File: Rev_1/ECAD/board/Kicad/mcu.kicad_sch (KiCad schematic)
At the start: 11 parts, among them Y100 16MHZ

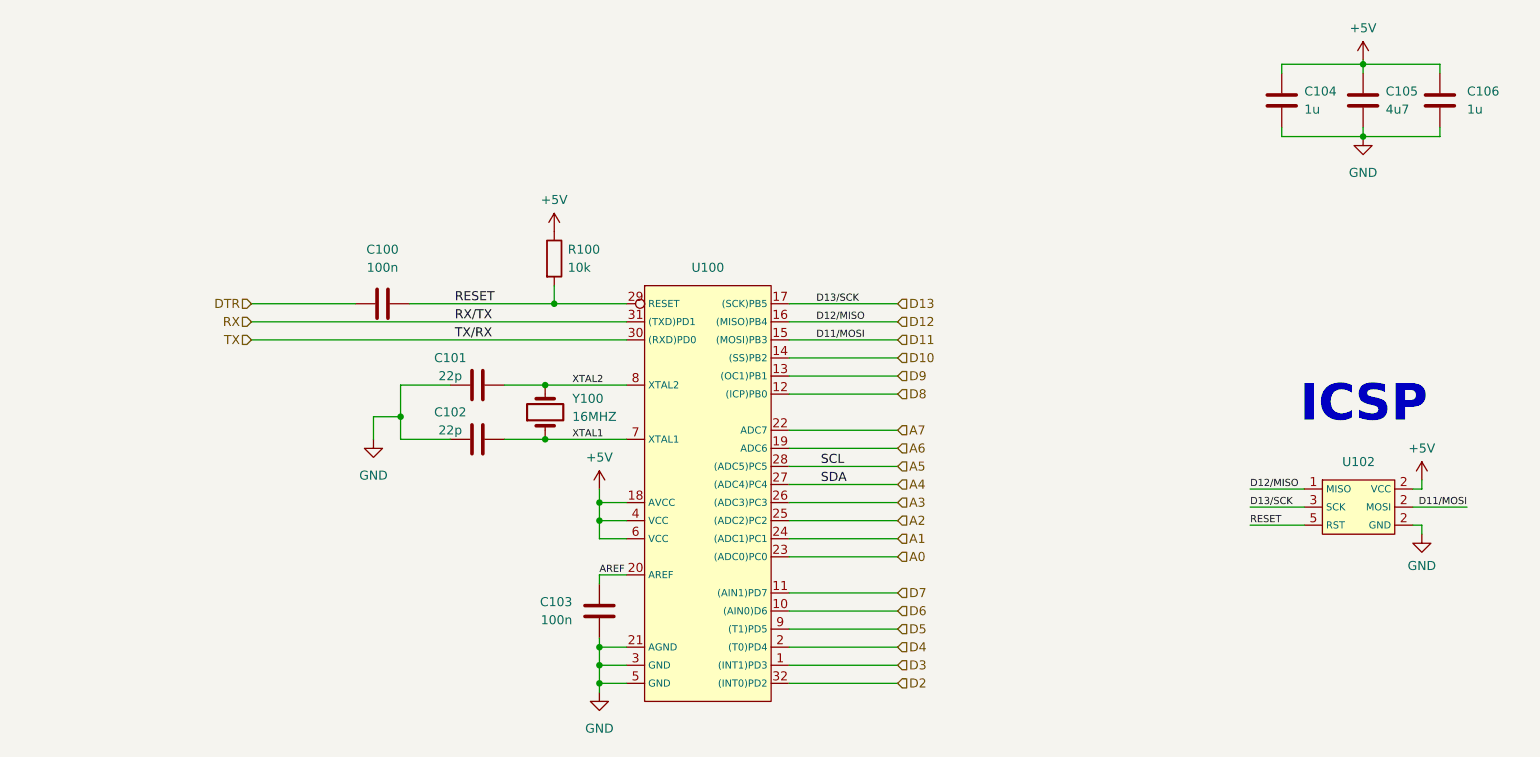
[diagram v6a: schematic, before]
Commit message: Updated gitignore
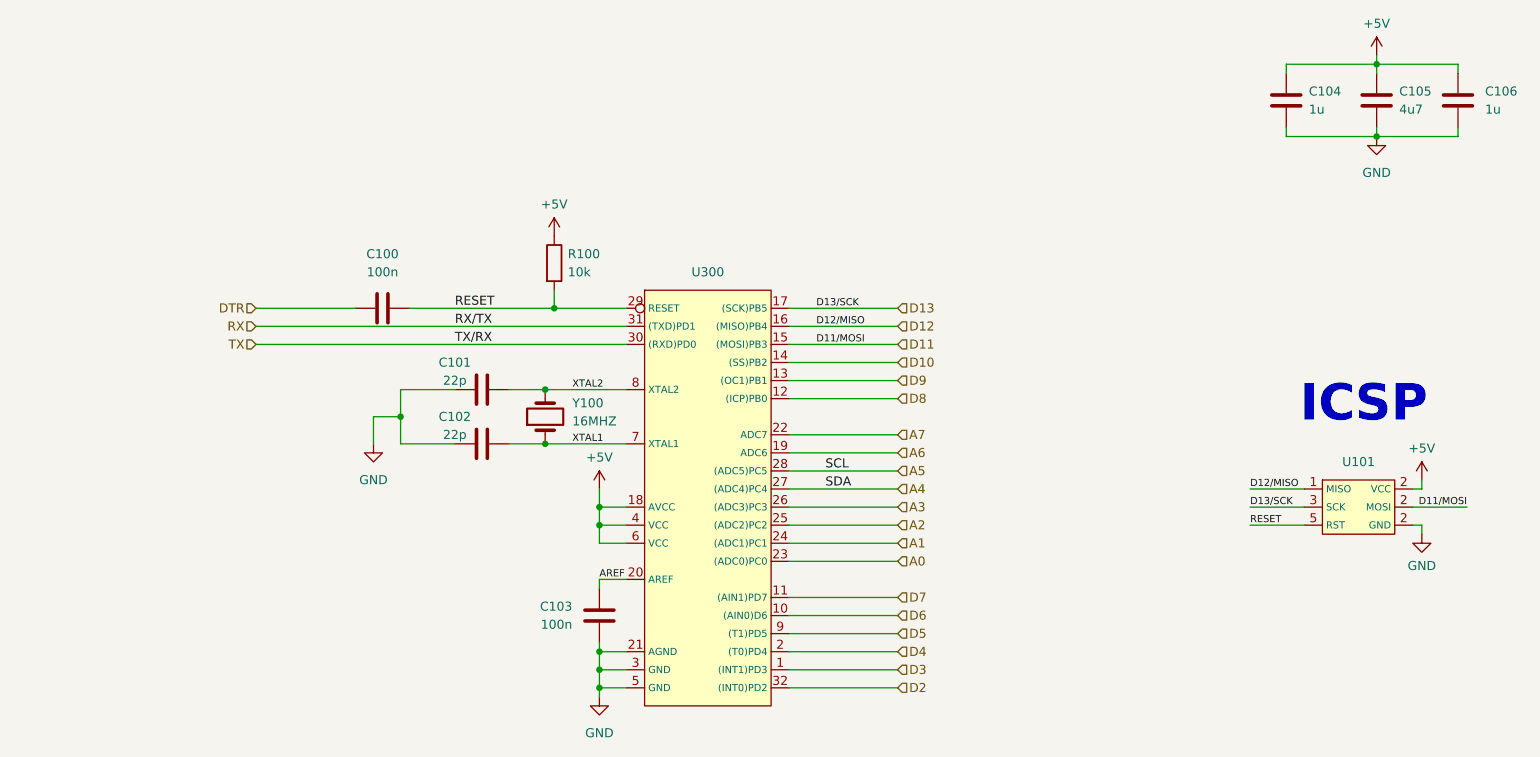
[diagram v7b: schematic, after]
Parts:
- removed U100: ~, symbol EEPROM_PROGRAMMER:ATMega328P-AU
- removed U102: ~, symbol EEPROM_PROGRAMMER:ICSP
- added U101: ~, symbol EEPROM_PROGRAMER:ICSP
- added U300: ~, symbol EEPROM_PROGRAMER:ATMega328P-AU
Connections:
- net +5V: now also U101.2 (VCC), U300.18 (AVCC), U300.4 (VCC), U300.6 (VCC)
- net A0: now also U300.23 ((ADC0)PC0)
- net A1: now also U300.24 ((ADC1)PC1)
- net A2: now also U300.25 ((ADC2)PC2)
- net A3: now also U300.26 ((ADC3)PC3)
- net A4: now also U300.27 ((ADC4)PC4)
- net A5: now also U300.28 ((ADC5)PC5)
- net A6: now also U300.19 (ADC6)
- net A7: now also U300.22 (ADC7)
- net AREF: now also U300.20 (AREF)
- net D10: now also U300.14 ((SS)PB2)
- net D11: now also U101.2 (VCC), U300.15 ((MOSI)PB3)
- net D12: now also U101.1 (MISO), U300.16 ((MISO)PB4)
- net D13: now also U101.3 (SCK), U300.17 ((SCK)PB5)
- net D2: now also U300.32 ((INT0)PD2)
- net D3: now also U300.1 ((INT1)PD3)
- net D4: now also U300.2 ((T0)PD4)
- net D5: now also U300.9 ((T1)PD5)
- net D6: now also U300.10 ((AIN0)D6)
- net D7: now also U300.11 ((AIN1)PD7)
- net D8: now also U300.12 ((ICP)PB0)
- net D9: now also U300.13 ((OC1)PB1)
- net GND: now also U101.2 (VCC), U300.21 (AGND), U300.3 (GND), U300.5 (GND)
- net RESET: now also U101.5 (RST), U300.29 (RESET)
- net RX: now also U300.31 ((TXD)PD1)
- net TX: now also U300.30 ((RXD)PD0)
- net XTAL1: now also U300.7 (XTAL1)
- net XTAL2: now also U300.8 (XTAL2)
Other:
- moved on the sheet: C100, C101, C102, C103, C104, C105, C106, R100, Y100
